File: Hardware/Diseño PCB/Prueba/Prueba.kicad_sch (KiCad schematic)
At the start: 2 parts

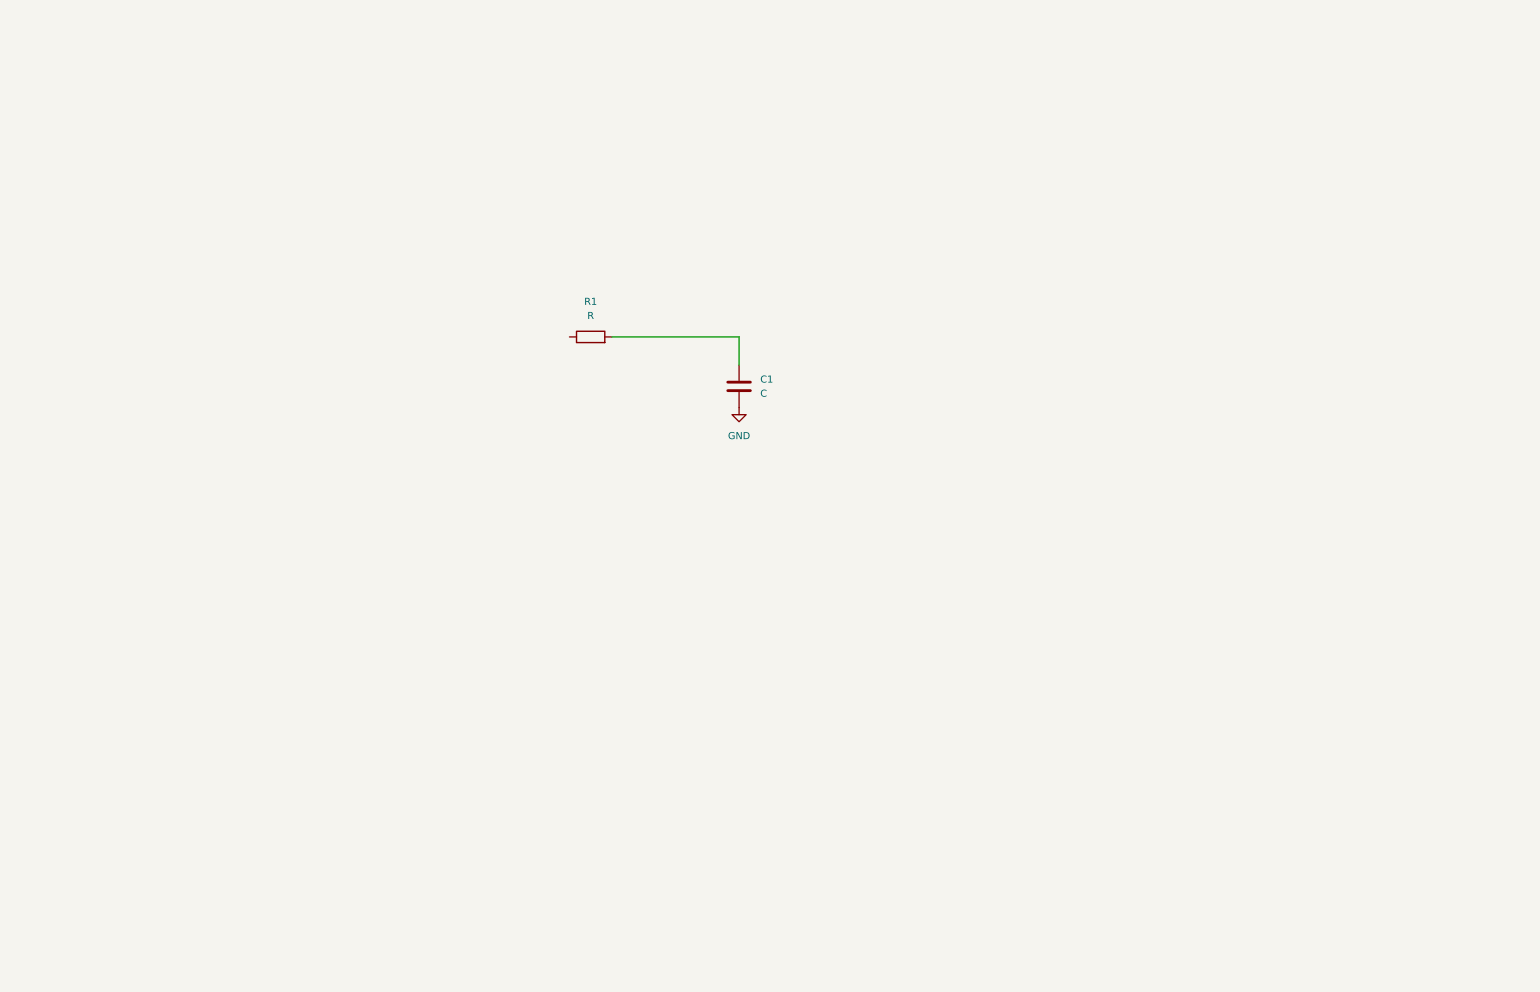
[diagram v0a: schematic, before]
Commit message: Arreglo pares diferenciales en el esquematico
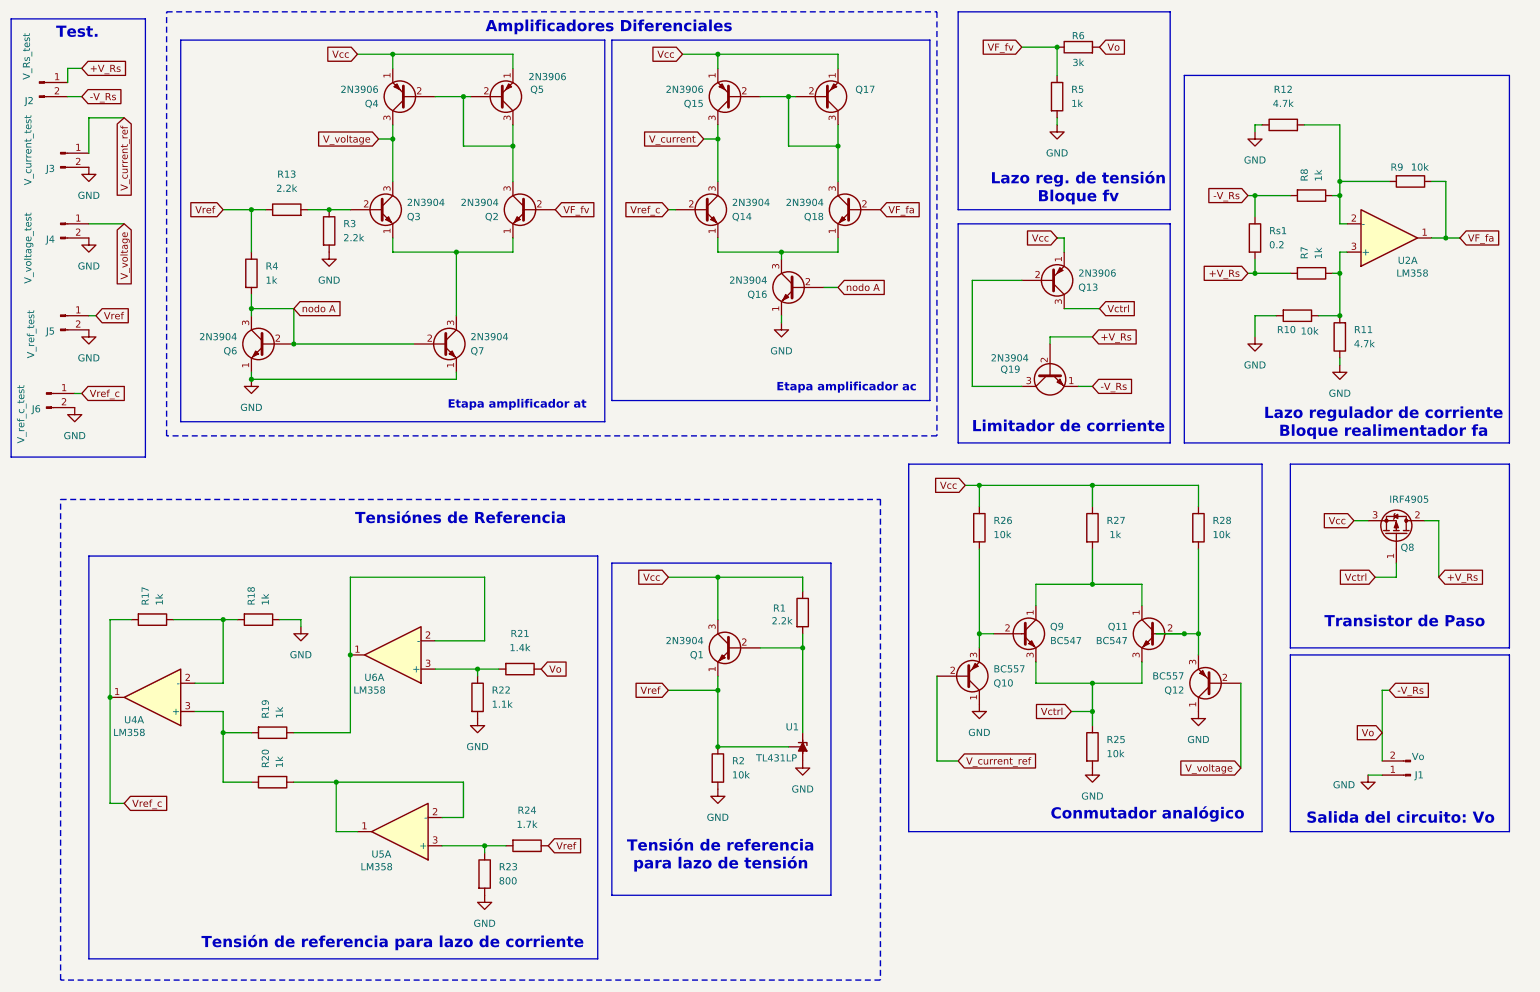
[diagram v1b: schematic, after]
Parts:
- removed C1: C, symbol Device:C
- added J1: Vo, symbol Connector:Conn_01x02_Pin
- added J2: V_Rs_test, symbol Connector:Conn_01x02_Pin
- added J3: V_current_test, symbol Connector:Conn_01x02_Pin
- added J4: V_voltage_test, symbol Connector:Conn_01x02_Pin
- added J5: V_ref_test, symbol Connector:Conn_01x02_Pin
- added J6: V_ref_c_test, symbol Connector:Conn_01x02_Pin
- added Q1, Q14, Q16, Q18, Q19, Q2, Q3, Q6, Q7: 2N3904, Package_TO_SOT_THT:TO-92_Inline, symbol Transistor_BJT:2N3904
- added Q10, Q12: BC557, Package_TO_SOT_THT:TO-92_Inline, symbol Transistor_BJT:BC557
- added Q11, Q9: BC547, Package_TO_SOT_THT:TO-92_Inline, symbol Transistor_BJT:BC547
- added Q13, Q15, Q17, Q4, Q5: 2N3906, Package_TO_SOT_THT:TO-92_Inline, symbol Transistor_BJT:2N3906
- added Q8: IRF4905, Package_TO_SOT_THT:TO-220-3_Vertical, symbol Transistor_FET:IRF4905
- added R10, R2, R25, R26, R28, R9: 10k, symbol Device:R
- added R11, R12: 4.7k, symbol Device:R
- added R13, R3: 2.2k, symbol Device:R
- added R17, R18, R19, R20, R27, R4, R5, R7, R8: 1k, symbol Device:R
- added R21: 1.4k, symbol Device:R
- added R22: 1.1k, symbol Device:R
- added R23: 800, symbol Device:R
- added R24: 1.7k, symbol Device:R
- added R6: 3k, symbol Device:R
- added Rs1: 0.2, symbol Device:R
- added U1: TL431LP, Package_TO_SOT_THT:TO-92_Inline, symbol Reference_Voltage:TL431LP
- added U2, U4, U5, U6: LM358, symbol Amplifier_Operational:LM358
- R1: value R -> 2.2k
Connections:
- net GND: now also J1.1 (Pin_1), J3.2 (Pin_2), J4.2 (Pin_2), J5.2 (Pin_2), J6.2 (Pin_2), Q10.1 (C), Q12.1 (C), Q16.1 (E), Q6.1 (E), Q7.1 (E), R10.2, R11.1, R12.1, R18.1, R2.2, R22.2, R23.2, R25.2, R3.2, R5.2, U1.2 (A)
- net Vcc: now reaches R1.1
- net Vcc: now also Q1.3 (C), Q13.1 (E), Q15.1 (E), Q17.1 (E), Q4.1 (E), Q5.1 (E), Q8.3 (S), R26.1, R27.1, R28.1
- net at R1.2: now also Q1.2 (B), U1.3 (K)
- new net: R12.2, R8.1, R9.2, U2.2 (-)
- new net: R10.1, R11.2, R7.1, U2.3 (+)
- new net: R19.1, U6.1, U6.2 (-)
- new net: R21.2, R22.1, U6.3 (+)
- new net: Q2.1 (E), Q3.1 (E), Q7.3 (C)
- new net: Q2.3 (C), Q4.2 (B), Q5.2 (B), Q5.3 (C)
- new net: Q11.2 (B), Q12.3 (E), R28.2
- new net: Q15.2 (B), Q17.2 (B), Q17.3 (C), Q18.3 (C)
- new net: Q13.2 (B), Q19.3 (C)
- new net: Q14.1 (E), Q16.3 (C), Q18.1 (E)
- new net: Q3.2 (B), R13.2, R3.1
- new net: R23.1, R24.2, U5.3 (+)
- new net: R20.1, U5.1, U5.2 (-)
- new net: Q11.1 (C), Q9.1 (C), R27.2
- new net: Q10.3 (E), Q9.2 (B), R26.2
- new net: R19.2, R20.2, U4.3 (+)
- new net: R17.1, R18.2, U4.2 (-)
- new net +V_Rs: J2.1 (Pin_1), Q19.2 (B), Q8.2 (D), R7.2, Rs1.2
- new net -V_Rs: J1.2 (Pin_2), J2.2 (Pin_2), Q19.1 (E), R21.1, R6.2, R8.2, Rs1.1
- new net VF_fa: Q18.2 (B), R9.1, U2.1
- new net VF_fv: Q2.2 (B), R5.1, R6.1
- new net V_current: Q14.3 (C), Q15.3 (C)
- new net V_current_ref: J3.1 (Pin_1), Q10.2 (B)
- new net V_voltage: J4.1 (Pin_1), Q12.2 (B), Q3.3 (C), Q4.3 (C)
- new net Vctrl: Q11.3 (E), Q13.3 (C), Q8.1 (G), Q9.3 (E), R25.1
- new net Vref: J5.1 (Pin_1), Q1.1 (E), R13.1, R2.1, R24.1, R4.1, U1.1 (REF)
- new net Vref_c: J6.1 (Pin_1), Q14.2 (B), R17.2, U4.1
- new net nodo A: Q16.2 (B), Q6.2 (B), Q6.3 (C), Q7.2 (B), R4.2
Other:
- note added: "Amplificadores Diferenciales"
- note added: "Conmutador analógico"
- note added: "Etapa amplificador ac"
- note added: "Etapa amplificador at"
- note added: "Lazo reg. de tensión Bloque fv"
- note added: "Lazo regulador de corriente Bloque realimentador fa"
- note added: "Limitador de corriente"
- note added: "Salida del circuito: Vo"
- note added: "Tensión de referencia para lazo de corriente"
- note added: "Tensión de referencia para lazo de tensión"
- note added: "Tensiónes de Referencia"
- note added: "Test."
- note added: "Transistor de Paso"
- company: (none) -> Grupo 7 - TA137
- title: (none) -> Regulador de baja caída (LDO,Low Dropout Regulator) 

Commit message: Planilla de compras actualizada, hojas de datos
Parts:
- J1, J2, J3, J4, J5, J6: footprint (none) -> Connector_PinHeader_2.00mm:PinHeader_1x01_P2.00mm_Vertical
- R1, R10, R11, R12, R13, R17, R18, R19, R2, R20, R21, R22, R23, R24, R25, R26, R27, R28, R3, R4, R5, R6, R7, R8, R9, Rs1: footprint (none) -> Resistor_THT:R_Axial_DIN0204_L3.6mm_D1.6mm_P7.62mm_Horizontal
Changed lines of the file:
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@@
 			)
 		)
-		(property "Footprint" ""
+		(property "Footprint" "Resistor_THT:R_Axial_DIN0204_L3.6mm_D1.6mm_P7.62mm_Horizontal"
 			(at 254.508 72.39 90)
 			(hide yes)
@@
 			)
 		)
-		(property "Footprint" ""
+		(property "Footprint" "Resistor_THT:R_Axial_DIN0204_L3.6mm_D1.6mm_P7.62mm_Horizontal"
 			(at 242.57 36.068 90)
 			(hide yes)
@@
 			)
 		)
-		(property "Footprint" ""
+		(property "Footprint" "Resistor_THT:R_Axial_DIN0204_L3.6mm_D1.6mm_P7.62mm_Horizontal"
 			(at 247.65 59.182 90)
 			(hide yes)
@@
 			)
 		)
-		(property "Footprint" ""
+		(property "Footprint" "Resistor_THT:R_Axial_DIN0204_L3.6mm_D1.6mm_P7.62mm_Horizontal"
 			(at 225.552 106.68 90)
 			(hide yes)
@@
 			)
 		)
-		(property "Footprint" ""
+		(property "Footprint" "Resistor_THT:R_Axial_DIN0204_L3.6mm_D1.6mm_P7.62mm_Horizontal"
 			(at 235.712 54.61 90)
 			(hide yes)
@@
 			)
 		)
-		(property "Footprint" ""
+		(property "Footprint" "Connector_PinHeader_2.00mm:PinHeader_1x01_P2.00mm_Vertical"
 			(at 22.86 39.37 0)
 			(hide yes)
@@
 			)
 		)
-		(property "Footprint" ""
+		(property "Footprint" "Resistor_THT:R_Axial_DIN0204_L3.6mm_D1.6mm_P7.62mm_Horizontal"
 			(at 205.74 22.098 90)
 			(hide yes)
@@
 			)
 		)
-		(property "Footprint" ""
+		(property "Footprint" "Resistor_THT:R_Axial_DIN0204_L3.6mm_D1.6mm_P7.62mm_Horizontal"
 			(at 63.5 51.308 90)
 			(hide yes)
@@
 			)
 		)
-		(property "Footprint" ""
+		(property "Footprint" "Resistor_THT:R_Axial_DIN0204_L3.6mm_D1.6mm_P7.62mm_Horizontal"
 			(at 154.432 121.92 90)
 			(hide yes)
@@
 			)
 		)
-		(property "Footprint" ""
+		(property "Footprint" "Resistor_THT:R_Axial_DIN0204_L3.6mm_D1.6mm_P7.62mm_Horizontal"
 			(at 106.68 162.052 90)
 			(hide yes)
@@
 			)
 		)
-		(property "Footprint" ""
+		(property "Footprint" "Resistor_THT:R_Axial_DIN0204_L3.6mm_D1.6mm_P7.62mm_Horizontal"
 			(at 206.502 146.05 90)
 			(hide yes)
@@
 			)
 		)
-		(property "Footprint" ""
+		(property "Footprint" "Connector_PinHeader_2.00mm:PinHeader_1x01_P2.00mm_Vertical"
 			(at 265.43 151.13 0)
 			(hide yes)
@@
 			)
 		)
-		(property "Footprint" ""
+		(property "Footprint" "Resistor_THT:R_Axial_DIN0204_L3.6mm_D1.6mm_P7.62mm_Horizontal"
 			(at 105.41 130.302 90)
 			(hide yes)
@@
 			)
 		)
-		(property "Footprint" ""
+		(property "Footprint" "Resistor_THT:R_Axial_DIN0204_L3.6mm_D1.6mm_P7.62mm_Horizontal"
 			(at 206.502 106.68 90)
 			(hide yes)
@@
 			)
 		)
-		(property "Footprint" ""
+		(property "Footprint" "Resistor_THT:R_Axial_DIN0204_L3.6mm_D1.6mm_P7.62mm_Horizontal"
 			(at 265.43 42.672 90)
 			(hide yes)
@@
 			)
 		)
-		(property "Footprint" ""
+		(property "Footprint" "Connector_PinHeader_2.00mm:PinHeader_1x01_P2.00mm_Vertical"
 			(at 22.86 52.07 0)
 			(hide yes)
@@
 			)
 		)
-		(property "Footprint" ""
+		(property "Footprint" "Resistor_THT:R_Axial_DIN0204_L3.6mm_D1.6mm_P7.62mm_Horizontal"
 			(at 186.182 106.68 90)
 			(hide yes)
@@
 			)
 		)
-		(property "Footprint" ""
+		(property "Footprint" "Connector_PinHeader_2.00mm:PinHeader_1x01_P2.00mm_Vertical"
 			(at 20.32 82.55 0)
 			(hide yes)
@@
 			)
 		)
-		(property "Footprint" ""
+		(property "Footprint" "Resistor_THT:R_Axial_DIN0204_L3.6mm_D1.6mm_P7.62mm_Horizontal"
 			(at 96.012 137.16 90)
 			(hide yes)
@@
 			)
 		)
-		(property "Footprint" ""
+		(property "Footprint" "Connector_PinHeader_2.00mm:PinHeader_1x01_P2.00mm_Vertical"
 			(at 19.05 26.67 0)
 			(hide yes)
@@
 			)
 		)
-		(property "Footprint" ""
+		(property "Footprint" "Resistor_THT:R_Axial_DIN0204_L3.6mm_D1.6mm_P7.62mm_Horizontal"
 			(at 60.96 141.732 90)
 			(hide yes)
@@
 			)
 		)
-		(property "Footprint" ""
+		(property "Footprint" "Resistor_THT:R_Axial_DIN0204_L3.6mm_D1.6mm_P7.62mm_Horizontal"
 			(at 69.342 53.34 90)
 			(hide yes)
@@
 			)
 		)
-		(property "Footprint" ""
+		(property "Footprint" "Resistor_THT:R_Axial_DIN0204_L3.6mm_D1.6mm_P7.62mm_Horizontal"
 			(at 247.65 45.212 90)
 			(hide yes)
@@
 			)
 		)
-		(property "Footprint" ""
+		(property "Footprint" "Resistor_THT:R_Axial_DIN0204_L3.6mm_D1.6mm_P7.62mm_Horizontal"
 			(at 97.282 168.91 90)
 			(hide yes)
@@
 			)
 		)
-		(property "Footprint" ""
+		(property "Footprint" "Resistor_THT:R_Axial_DIN0204_L3.6mm_D1.6mm_P7.62mm_Horizontal"
 			(at 139.192 149.86 90)
 			(hide yes)
@@
 			)
 		)
-		(property "Footprint" ""
+		(property "Footprint" "Resistor_THT:R_Axial_DIN0204_L3.6mm_D1.6mm_P7.62mm_Horizontal"
 			(at 245.11 66.802 90)
 			(hide yes)
@@
 			)
 		)
-		(property "Footprint" ""
+		(property "Footprint" "Resistor_THT:R_Axial_DIN0204_L3.6mm_D1.6mm_P7.62mm_Horizontal"
 			(at 58.42 121.412 90)
 			(hide yes)
@@
 			)
 		)
-		(property "Footprint" ""
+		(property "Footprint" "Resistor_THT:R_Axial_DIN0204_L3.6mm_D1.6mm_P7.62mm_Horizontal"
 			(at 60.96 150.622 90)
 			(hide yes)
@@
 			)
 		)
-		(property "Footprint" ""
+		(property "Footprint" "Resistor_THT:R_Axial_DIN0204_L3.6mm_D1.6mm_P7.62mm_Horizontal"
 			(at 55.372 60.96 90)
 			(hide yes)
@@
 			)
 		)
-		(property "Footprint" ""
+		(property "Footprint" "Resistor_THT:R_Axial_DIN0204_L3.6mm_D1.6mm_P7.62mm_Horizontal"
 			(at 39.37 121.412 90)
 			(hide yes)
@@
 			)
 		)
-		(property "Footprint" ""
+		(property "Footprint" "Resistor_THT:R_Axial_DIN0204_L3.6mm_D1.6mm_P7.62mm_Horizontal"
 			(at 200.152 29.21 90)
 			(hide yes)
@@
 			)
 		)
-		(property "Footprint" ""
+		(property "Footprint" "Connector_PinHeader_2.00mm:PinHeader_1x01_P2.00mm_Vertical"
 			(at 22.86 68.58 0)
 			(hide yes)

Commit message: huellas de componentes ok
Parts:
- removed U4, U5, U6: LM358, symbol Amplifier_Operational:LM358
- added unit 3 of U2
- added unit 2 of U2
- added U3: LM358, Package_DIP:DIP-8_W7.62mm, symbol Amplifier_Operational:LM358
- U2: footprint (none) -> Package_DIP:DIP-8_W7.62mm
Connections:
- net Vref_c: now also U3.7
- net at R12.2, R8.1, R9.2: now also U2.3 (+); no longer U2.2 (-)
- net at R10.1, R11.2, R7.1: now also U2.2 (-); no longer U2.3 (+)
- net at R19.1: now also U2.6 (-), U2.7
- net at R21.2, R22.1: now also U2.5 (+)
- net at R23.1, R24.2: now also U3.3 (+)
- net at R20.1: now also U3.1, U3.2 (-)
- net at R19.2, R20.2: now also U3.5 (+)
- net at R17.1, R18.2: now also U3.6 (-)
